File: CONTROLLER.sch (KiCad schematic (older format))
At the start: 25 parts, among them J201 Raspberry_Pi_2_3, Q201 BSS138, Q202 BSS138, U201 MCP23017_SO, U202 MAX11616, U203 MAX3232

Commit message: Review 1
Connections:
- net +5V: now also C202.1; no longer C202.2
- net Earth: now also C202.2; no longer C202.1
- net ILK_CMD renamed ILK_CMD_PI
- net OP renamed OP_CMD_PI
- net RESET_CMD renamed RESET_CMD_PI
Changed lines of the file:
@@
 Sheet 2 4
 Title "RF Amplifier Controller"
-Date "2019-11-23"
+Date "2019-12-01"
 Rev "1"
 Comp "HB9GKW"
@@
 ILK_RF_OL
 Text GLabel 10075 5425 2    50   Output ~ 0
-RESET_CMD
+RESET_CMD_PI
 Text GLabel 3925 7475 0    50   Input ~ 0
 ILK_IDD_OC
@@
 	4925 3675 5050 3675
 Connection ~ 4925 3675
-Wire Wire Line
-	4925 3675 4925 3300
 $Comp
 L power:Earth #PWR?
@@
 	9225 7050 9325 7050
 Text GLabel 10075 5325 2    50   Output ~ 0
-OP
+OP_CMD_PI
 Wire Wire Line
 	10075 5325 9925 5325
 Text GLabel 10075 5525 2    50   Output ~ 0
-ILK_CMD
+ILK_CMD_PI
 Wire Wire Line
 	10075 5525 9925 5525
@@
 AR Path="/5DD09976" Ref="C?"  Part="1"
 AR Path="/5CBD59C6/5DD09976" Ref="C202"  Part="1"
-F 0 "C202" V 4975 3250 50  0000 L CNN
-F 1 "10u" V 5050 3200 50  0000 L CNN
+F 0 "C202" V 5425 3200 50  0000 L CNN
+F 1 "10u" V 5350 3225 50  0000 L CNN
 F 2 "Capacitor_Tantalum_SMD:CP_EIA-6032-28_Kemet-C" H 5238 3150 50  0001 C CNN
 F 3 "~" H 5200 3300 50  0001 C CNN
 	1    5200 3300
-	0    1    1    0
+	0    -1   -1   0
 $EndComp
 $Comp
@@
 	0    -1   -1   0
 $EndComp
-Wire Wire Line
-	5050 3300 4925 3300
-Connection ~ 4925 3300
-Wire Wire Line
-	4925 3300 4925 3175
 Wire Notes Line
 	7925 8050 7925 9825
@@
 	9025 7025 9025 7075
 NoConn ~ 8925 7025
+Wire Wire Line
+	4925 3175 4925 3300
+Wire Wire Line
+	5050 3300 4925 3300
+Connection ~ 4925 3300
+Wire Wire Line
+	4925 3300 4925 3675
 $EndSCHEMATC

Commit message: Review
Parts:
- C202: value 10u -> 47u
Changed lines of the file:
@@
 Sheet 2 4
 Title "RF Amplifier Controller"
-Date "2019-12-01"
+Date "2020-01-19"
 Rev "1"
 Comp "HB9GKW"
@@
 U 1 1 5E639734
 P 5175 5750
-F 0 "C201" V 5400 5650 50  0000 L CNN
-F 1 "100n" V 5325 5650 50  0000 L CNN
+F 0 "C201" V 5375 5650 50  0000 L CNN
+F 1 "100n" V 5300 5650 50  0000 L CNN
 F 2 "Capacitor_SMD:C_0805_2012Metric_Pad1.15x1.40mm_HandSolder" H 5213 5600 50  0001 C CNN
 F 3 "~" H 5175 5750 50  0001 C CNN
@@
 AR Path="/5CBD59C6/5DC48293" Ref="U203"  Part="1"
 AR Path="/5DC48293" Ref="U?"  Part="1"
-F 0 "U203" H 11850 7050 50  0000 C CNN
+F 0 "U203" H 11900 7050 50  0000 C CNN
 F 1 "MAX3232" H 11975 6950 50  0000 C CNN
 F 2 "Package_SO:SOIC-18W_7.5x11.6mm_P1.27mm" H 12450 4850 50  0001 L CNN
@@
 U 1 1 5DC62099
 P 11525 5150
-F 0 "C205" H 11275 5225 50  0000 L CNN
-F 1 "100n" H 11200 5125 50  0000 L CNN
+F 0 "C205" H 11225 5200 50  0000 L CNN
+F 1 "100n" H 11225 5100 50  0000 L CNN
 F 2 "Capacitor_SMD:C_0805_2012Metric_Pad1.15x1.40mm_HandSolder" H 11563 5000 50  0001 C CNN
 F 3 "~" H 11525 5150 50  0001 C CNN
@@
 U 1 1 5DC9523F
 P 13275 5150
-F 0 "C207" H 13025 5225 50  0000 L CNN
-F 1 "100n" H 12950 5125 50  0000 L CNN
+F 0 "C207" H 12975 5200 50  0000 L CNN
+F 1 "100n" H 12975 5100 50  0000 L CNN
 F 2 "Capacitor_SMD:C_0805_2012Metric_Pad1.15x1.40mm_HandSolder" H 13313 5000 50  0001 C CNN
 F 3 "~" H 13275 5150 50  0001 C CNN
@@
 U 1 1 5DE06F4A
 P 13475 5800
-F 0 "C209" V 13600 5975 50  0000 L CNN
+F 0 "C209" V 13600 5875 50  0000 L CNN
 F 1 "100n" V 13525 5875 50  0000 L CNN
 F 2 "Capacitor_SMD:C_0805_2012Metric_Pad1.15x1.40mm_HandSolder" H 13513 5650 50  0001 C CNN
@@
 U 1 1 5DE10581
 P 13475 5500
-F 0 "C208" V 13600 5675 50  0000 L CNN
+F 0 "C208" V 13600 5575 50  0000 L CNN
 F 1 "100n" V 13525 5575 50  0000 L CNN
 F 2 "Capacitor_SMD:C_0805_2012Metric_Pad1.15x1.40mm_HandSolder" H 13513 5350 50  0001 C CNN
@@
 AR Path="/5DE667F3" Ref="R?"  Part="1"
 AR Path="/5CBD59C6/5DE667F3" Ref="R207"  Part="1"
-F 0 "R207" H 9445 8671 50  0000 L CNN
-F 1 "1k8" H 9445 8580 50  0000 L CNN
+F 0 "R207" V 9475 8525 50  0000 L CNN
+F 1 "1k8" V 9550 8550 50  0000 L CNN
 F 2 "Resistor_SMD:R_0805_2012Metric_Pad1.15x1.40mm_HandSolder" V 9305 8625 50  0001 C CNN
 F 3 "~" H 9375 8625 50  0001 C CNN
@@
 AR Path="/5DEA4FD4" Ref="R?"  Part="1"
 AR Path="/5CBD59C6/5DEA4FD4" Ref="R208"  Part="1"
-F 0 "R208" H 9445 9296 50  0000 L CNN
-F 1 "1k8" H 9445 9205 50  0000 L CNN
+F 0 "R208" V 9475 9150 50  0000 L CNN
+F 1 "1k8" V 9550 9175 50  0000 L CNN
 F 2 "Resistor_SMD:R_0805_2012Metric_Pad1.15x1.40mm_HandSolder" V 9305 9250 50  0001 C CNN
 F 3 "~" H 9375 9250 50  0001 C CNN
@@
 AR Path="/5DECE479" Ref="R?"  Part="1"
 AR Path="/5CBD59C6/5DECE479" Ref="R204"  Part="1"
-F 0 "R204" H 8325 8675 50  0000 L CNN
-F 1 "2k7" H 8300 8575 50  0000 L CNN
+F 0 "R204" V 8350 8525 50  0000 L CNN
+F 1 "2k7" V 8425 8550 50  0000 L CNN
 F 2 "Resistor_SMD:R_0805_2012Metric_Pad1.15x1.40mm_HandSolder" V 8430 8625 50  0001 C CNN
 F 3 "~" H 8500 8625 50  0001 C CNN
@@
 AR Path="/5DEE53F9" Ref="R?"  Part="1"
 AR Path="/5CBD59C6/5DEE53F9" Ref="R205"  Part="1"
-F 0 "R205" H 8325 9300 50  0000 L CNN
-F 1 "2k7" H 8300 9200 50  0000 L CNN
+F 0 "R205" V 8350 9150 50  0000 L CNN
+F 1 "2k7" V 8425 9175 50  0000 L CNN
 F 2 "Resistor_SMD:R_0805_2012Metric_Pad1.15x1.40mm_HandSolder" V 8430 9250 50  0001 C CNN
 F 3 "~" H 8500 9250 50  0001 C CNN
@@
 AR Path="/5F47BFDA" Ref="R?"  Part="1"
 AR Path="/5CBD59C6/5F47BFDA" Ref="R202"  Part="1"
-F 0 "R202" H 5900 7500 50  0000 L CNN
-F 1 "2k2" H 5900 7400 50  0000 L CNN
+F 0 "R202" V 5950 7325 50  0000 L CNN
+F 1 "2k2" V 6025 7350 50  0000 L CNN
 F 2 "Resistor_SMD:R_0805_2012Metric_Pad1.15x1.40mm_HandSolder" V 5780 7425 50  0001 C CNN
 F 3 "~" H 5850 7425 50  0001 C CNN
@@
 AR Path="/5F4B73FB" Ref="R?"  Part="1"
 AR Path="/5CBD59C6/5F4B73FB" Ref="R201"  Part="1"
-F 0 "R201" H 5900 7200 50  0000 L CNN
-F 1 "2k2" H 5900 7100 50  0000 L CNN
+F 0 "R201" V 5700 7025 50  0000 L CNN
+F 1 "2k2" V 5775 7050 50  0000 L CNN
 F 2 "Resistor_SMD:R_0805_2012Metric_Pad1.15x1.40mm_HandSolder" V 5780 7125 50  0001 C CNN
 F 3 "~" H 5850 7125 50  0001 C CNN
@@
 U 1 1 5F4E9E98
 P 5900 6675
-F 0 "D201" H 6050 6425 50  0000 C CNN
-F 1 "BAT54AW" H 6100 6500 50  0000 C CNN
+F 0 "D201" H 5475 6650 50  0000 C CNN
+F 1 "BAT54AW" H 5400 6750 50  0000 C CNN
 F 2 "Package_TO_SOT_SMD:SOT-323_SC-70" H 5975 6800 50  0001 L CNN
 F 3 "https://assets.nexperia.com/documents/data-sheet/BAT54W_SER.pdf" H 5780 6675 50  0001 C CNN
@@
 AR Path="/5F5070BD" Ref="R?"  Part="1"
 AR Path="/5CBD59C6/5F5070BD" Ref="R203"  Part="1"
-F 0 "R203" H 6245 6296 50  0000 L CNN
-F 1 "1k5" H 6245 6205 50  0000 L CNN
+F 0 "R203" V 6275 6150 50  0000 L CNN
+F 1 "1k5" V 6350 6175 50  0000 L CNN
 F 2 "Resistor_SMD:R_0805_2012Metric_Pad1.15x1.40mm_HandSolder" V 6105 6250 50  0001 C CNN
 F 3 "~" H 6175 6250 50  0001 C CNN
@@
 AR Path="/5CBD59C6/5DD09976" Ref="C202"  Part="1"
 F 0 "C202" V 5425 3200 50  0000 L CNN
-F 1 "10u" V 5350 3225 50  0000 L CNN
+F 1 "47u" V 5350 3225 50  0000 L CNN
 F 2 "Capacitor_Tantalum_SMD:CP_EIA-6032-28_Kemet-C" H 5238 3150 50  0001 C CNN
 F 3 "~" H 5200 3300 50  0001 C CNN

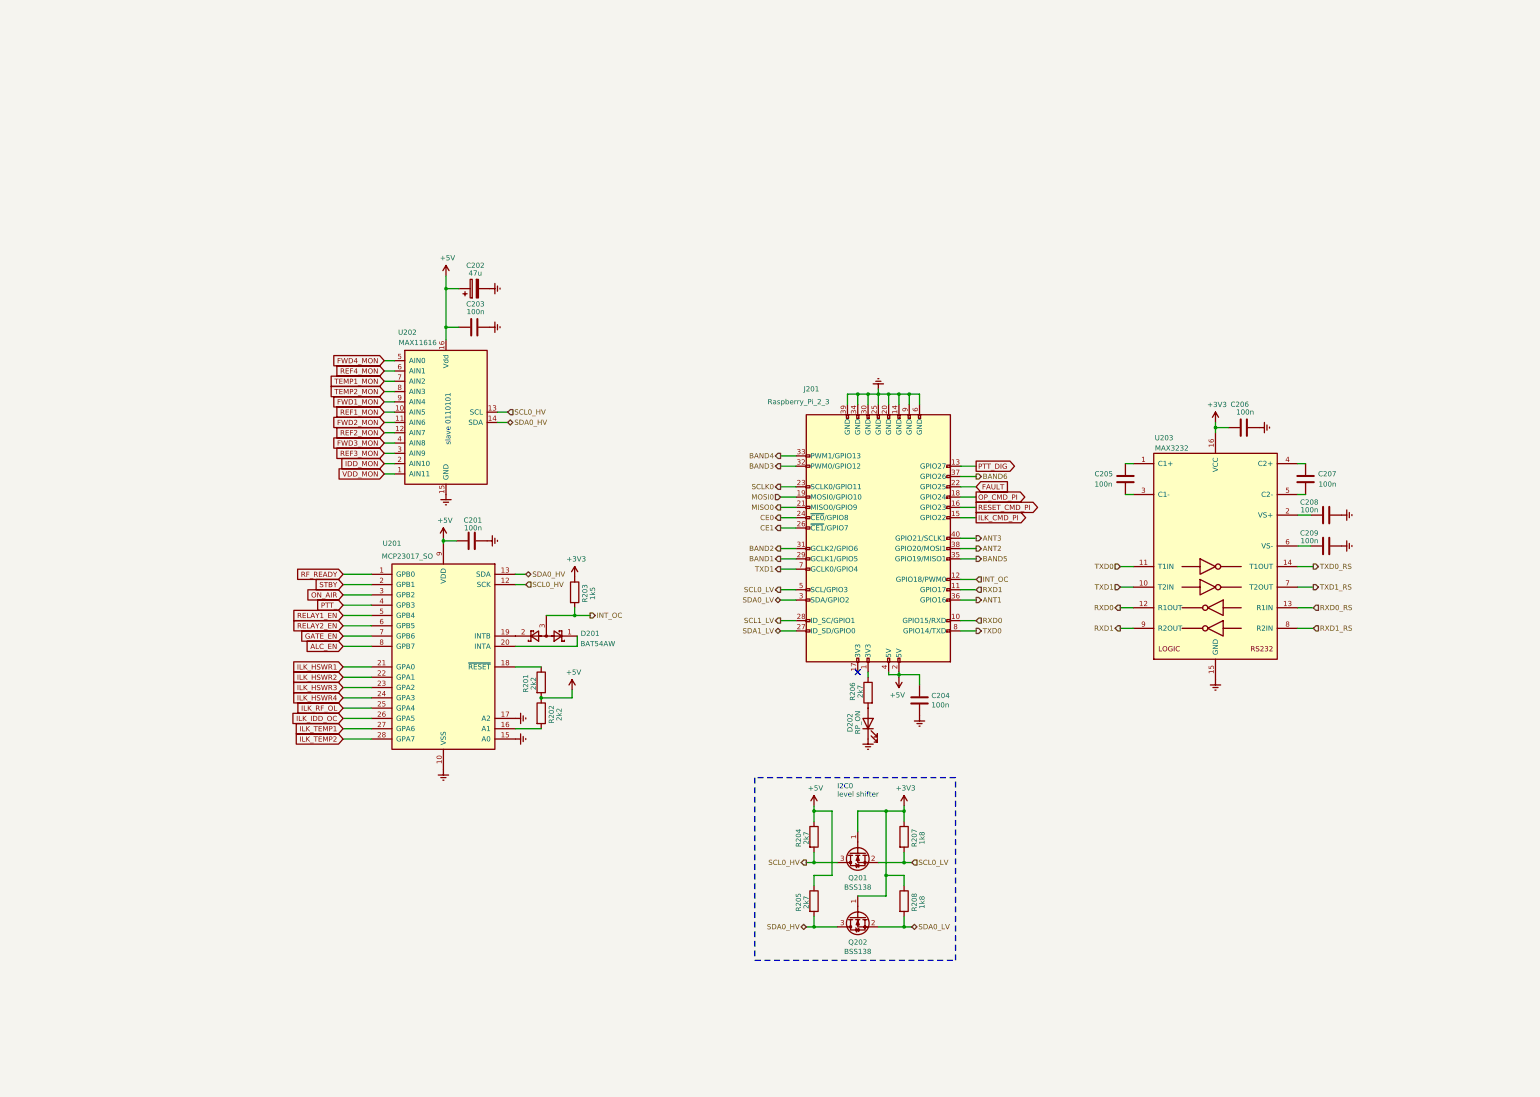
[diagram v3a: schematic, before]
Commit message: new Version with AVR Controller
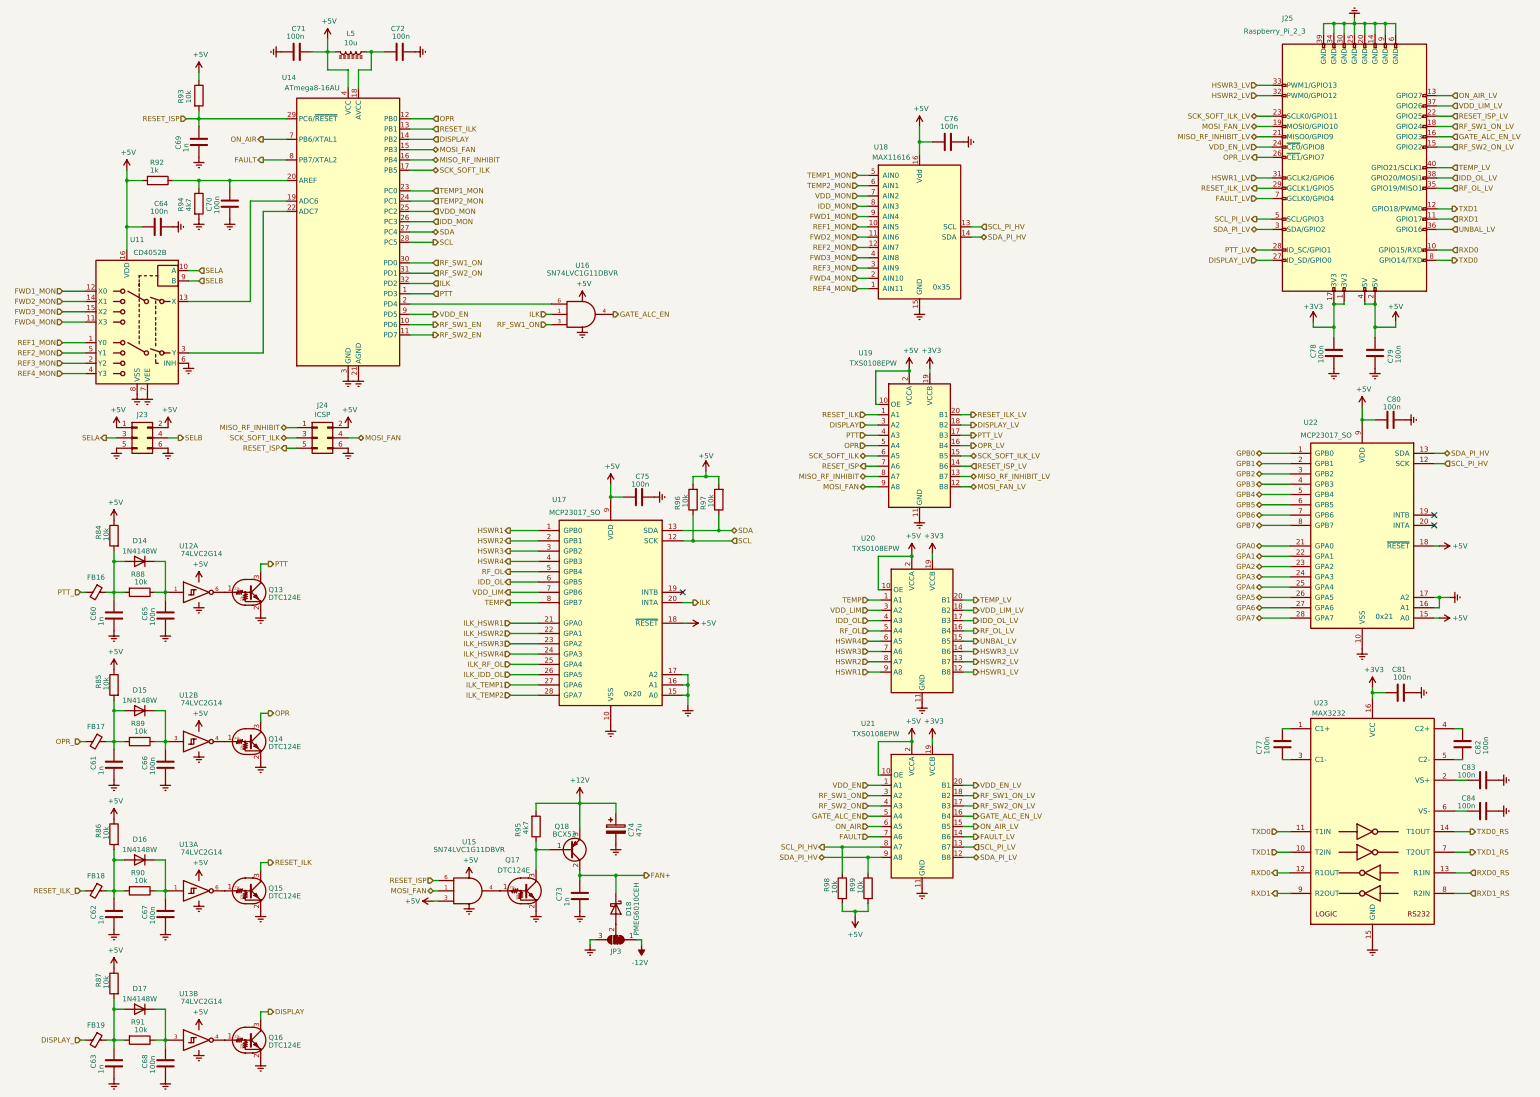
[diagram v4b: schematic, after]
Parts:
- removed C202: 47u, Capacitor_Tantalum_SMD:CP_EIA-6032-28_Kemet-C, symbol Device:CP
- removed D201: BAT54AW, Package_TO_SOT_SMD:SOT-323_SC-70, symbol Diode:BAT54AW
- removed D202: RP_ON, LED_THT:LED_D3.0mm, symbol Device:LED
- removed Q201, Q202: BSS138, Package_TO_SOT_SMD:SOT-23, symbol Transistor_FET:BSS138
- removed R201, R202: 2k2, Resistor_SMD:R_0805_2012Metric_Pad1.15x1.40mm_HandSolder, symbol Device:R
- removed R203: 1k5, Resistor_SMD:R_0805_2012Metric_Pad1.15x1.40mm_HandSolder, symbol Device:R
- removed R204, R205, R206: 2k7, Resistor_SMD:R_0805_2012Metric_Pad1.15x1.40mm_HandSolder, symbol Device:R
- removed R207, R208: 1k8, Resistor_SMD:R_0805_2012Metric_Pad1.15x1.40mm_HandSolder, symbol Device:R
- added C60, C61, C62, C63, C69, C73: 1n, Capacitor_SMD:C_0805_2012Metric_Pad1.15x1.40mm_HandSolder, symbol Device:C
- added C64, C65, C66, C67, C68, C70, C71, C72, C78, C80: 100n, Capacitor_SMD:C_0805_2012Metric_Pad1.15x1.40mm_HandSolder, symbol Device:C
- added C74: 47u, Capacitor_Tantalum_SMD:CP_EIA-6032-28_Kemet-C, symbol Device:CP
- added D14, D15, D16, D17: 1N4148W, Diode_SMD:D_SOD-123, symbol Diode:1N4148W
- added D18: PMEG6010CEH, Diode_SMD:D_SOD-123, symbol Diode:PMEG6010CEH
- added FB16, FB17, FB18, FB19: Ferrite_Bead_Small, Resistor_SMD:R_0805_2012Metric_Pad1.15x1.40mm_HandSolder, symbol Device:Ferrite_Bead_Small
- added J23: Conn_02x03_Odd_Even, Connector_PinHeader_2.54mm:PinHeader_2x03_P2.54mm_Vertical, symbol Connector_Generic:Conn_02x03_Odd_Even
- added J24: ICSP, Connector_PinHeader_2.54mm:PinHeader_2x03_P2.54mm_Vertical, symbol Connector_Generic:Conn_02x03_Odd_Even
- added JP3: SolderJumper_3_Bridged12, Jumper:SolderJumper-3_P1.3mm_Open_RoundedPad1.0x1.5mm, symbol Jumper:SolderJumper_3_Bridged12
- added L5: 10u, Inductor_SMD:L_0805_2012Metric, symbol Device:L_Core_Ferrite
- added Q13, Q14, Q15, Q16, Q17: DTC124E, Package_TO_SOT_SMD:SOT-23, symbol Transistor_BJT:DTC124E
- added Q18: BCX53, Package_TO_SOT_SMD:SOT-89-3, symbol Transistor_BJT:BCX53
- added R84, R85, R86, R87, R88, R89, R90, R91, R93, R96, R97, R98, R99: 10k, Resistor_SMD:R_0805_2012Metric_Pad1.15x1.40mm_HandSolder, symbol Device:R
- added R92: 1k, Resistor_SMD:R_0805_2012Metric_Pad1.15x1.40mm_HandSolder, symbol Device:R
- added R94, R95: 4k7, Resistor_SMD:R_0805_2012Metric_Pad1.15x1.40mm_HandSolder, symbol Device:R
- added U11: CD4052B, Package_SO:SOIC-16_3.9x9.9mm_P1.27mm, symbol Analog_Switch:CD4052B
- added U12, U13: 74LVC2G14, Package_TO_SOT_SMD:SOT-23-6, symbol 74xGxx:74LVC2G14
- added U14: ATmega8-16AU, Package_QFP:TQFP-32_7x7mm_P0.8mm, symbol MCU_Microchip_ATmega:ATmega8-16AU
- added U15, U16: SN74LVC1G11DBVR, Package_TO_SOT_SMD:SOT-23-6, symbol 74xGxx:74LVC1G11
- added U19, U20, U21: TXS0108EPW, Package_SO:TSSOP-20_4.4x6.5mm_P0.65mm, symbol Logic_LevelTranslator:TXS0108EPW
- added U22: MCP23017_SO, Package_SO:SOIC-28W_7.5x17.9mm_P1.27mm, symbol Interface_Expansion:MCP23017_SO
- renumbered C201 to C75, C203 to C76, C205 to C77, C204 to C79, C206 to C81, C207 to C82, C208 to C83, C209 to C84, J201 to J25, U201 to U17, U202 to U18, U203 to U23
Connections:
- net INT_OC is gone; now on net TXD1: J25.12 (GPIO18/PWM0)
- net +3V3: now also J25.1 (3V3), J25.17 (3V3), C78.1, U19.19 (VCCB), U20.19 (VCCB), U21.19 (VCCB)
- net +5V: now also U17.18 (~RESET~), C64.1, C71.1, C80.1, J23.1 (Pin_1), J23.2 (Pin_2), J24.2 (Pin_2), L5.2, R84.1, R85.1, R86.1, R87.1, R92.2, R93.1, R96.2, R97.2, R98.2, R99.2, U11.16 (VDD), U12.5 (VCC), U12.5 (VCC), U13.5 (VCC), U13.5 (VCC), U14.4 (VCC), U14.6 (VCC), U15.3, U15.5 (VCC), U16.5 (VCC), U19.10 (OE), U19.2 (VCCA), U20.10 (OE), U20.2 (VCCA), U21.10 (OE), U21.2 (VCCA), U22.15 (A0), U22.18 (~RESET~), U22.9 (VDD)
- net Earth: now also U17.16 (A1), C60.2, C61.2, C62.2, C63.2, C64.2, C65.2, C66.2, C67.2, C68.2, C69.2, C70.2, C71.2, C72.2, C73.2, C74.2, C78.2, C80.2, J23.5 (Pin_5), J23.6 (Pin_6), J24.6 (Pin_6), JP3.3 (B), Q13.2 (E), Q14.2 (E), Q15.2 (E), Q16.2 (E), Q17.2 (E), R94.2, U11.6 (INH), U11.7 (VEE), U11.8 (VSS), U12.2 (GND), U12.2 (GND), U13.2 (GND), U13.2 (GND), U14.21 (AGND), U14.3 (GND), U14.5 (GND), U15.2 (GND), U16.2 (GND), U19.11 (GND), U20.11 (GND), U21.11 (GND), U22.10 (VSS), U22.16 (A1), U22.17 (A2)
- net FAULT: now also U14.8 (PB7/XTAL2), U21.7 (A6); no longer J25.22 (GPIO25)
- net FWD1_MON: now also U11.12 (X0)
- net FWD2_MON: now also U11.14 (X1)
- net FWD3_MON: now also U11.15 (X2)
- net FWD4_MON: now also U18.2 (AIN10), U11.11 (X3); no longer U18.5 (AIN0)
- net IDD_MON: now also U18.8 (AIN3), U14.26 (PC3); no longer U18.2 (AIN10)
- net ON_AIR: now also U14.7 (PB6/XTAL1), U21.6 (A5); no longer U17.3 (GPB2)
- net PTT_: now also FB16.2; no longer U17.4 (GPB3)
- net REF1_MON: now also U11.1 (Y0)
- net REF2_MON: now also U11.5 (Y1)
- net REF3_MON: now also U11.2 (Y2)
- net REF4_MON: now also U18.1 (AIN11), U11.4 (Y3); no longer U18.6 (AIN1)
- net TEMP1_MON: now also U18.5 (AIN0), U14.23 (PC0); no longer U18.7 (AIN2)
- net TEMP2_MON: now also U18.6 (AIN1), U14.24 (PC1); no longer U18.8 (AIN3)
- net TXD1: no longer J25.7 (GCLK0/GPIO4)
- net VDD_MON: now also U18.7 (AIN2), U14.25 (PC2); no longer U18.1 (AIN11)
- net ILK: now reaches U17.20 (INTA)
- net ILK: now also U14.32 (PD2), U16.1
- net ALC_EN renamed TEMP
- net TEMP: now also U20.1 (A1)
- net ANT1 renamed UNBAL_LV
- net UNBAL_LV: now also U20.15 (B5)
- net ANT2 renamed IDD_OL_LV
- net IDD_OL_LV: now also U20.17 (B3)
- net ANT3 renamed TEMP_LV
- net TEMP_LV: now also U20.20 (B1)
- net BAND1 renamed RESET_ILK_LV
- net RESET_ILK_LV: now also U19.20 (B1)
- net BAND2 renamed HSWR1_LV
- net HSWR1_LV: now also U20.12 (B8)
- net BAND3 renamed HSWR2_LV
- net HSWR2_LV: now also U20.13 (B7)
- net BAND4 renamed HSWR3_LV
- net HSWR3_LV: now also U20.14 (B6)
- net BAND5 renamed RF_OL_LV
- net RF_OL_LV: now also U20.16 (B4)
- net BAND6 renamed VDD_LIM_LV
- net VDD_LIM_LV: now also U20.18 (B2)
- net CE0 renamed VDD_EN_LV
- net VDD_EN_LV: now also U21.20 (B1)
- net CE1 renamed OPR_LV
- net OPR_LV: now also U19.16 (B4)
- net GATE_EN renamed VDD_LIM
- net VDD_LIM: now also U20.3 (A2)
- net ILK_CMD_PI renamed RF_SW2_ON_LV
- net RF_SW2_ON_LV: now also U21.17 (B3)
- net ILK_IDD_OC renamed ILK_IDD_OL
- net MISO0 renamed MISO_RF_INHIBIT_LV
- net MISO_RF_INHIBIT_LV: now also U19.13 (B7)
- net MOSI0 renamed MOSI_FAN_LV
- net MOSI_FAN_LV: now also U19.12 (B8)
- net OP_CMD_PI renamed RF_SW1_ON_LV
- net RF_SW1_ON_LV: now also U21.18 (B2)
- net PTT_DIG renamed ON_AIR_LV
- net ON_AIR_LV: now also U21.15 (B5)
- net RELAY1_EN renamed RF_OL
- net RF_OL: now also U20.5 (A4)
- net RELAY2_EN renamed IDD_OL
- net IDD_OL: now also U20.4 (A3)
- net RESET_CMD_PI renamed GATE_ALC_EN_LV
- net GATE_ALC_EN_LV: now also U21.16 (B4)
- net RF_READY renamed HSWR1
- net HSWR1: now also U20.9 (A8)
- net SCL0_HV renamed SCL
- net SCL: now also R96.1, U14.28 (PC5); no longer U18.13 (SCL)
- net SCL0_LV renamed SCL_PI_LV
- net SCL_PI_LV: now also U21.13 (B7)
- net SCL1_LV renamed PTT_LV
- net PTT_LV: now also U19.17 (B3)
- net SCLK0 renamed SCK_SOFT_ILK_LV
- net SCK_SOFT_ILK_LV: now also U19.15 (B5)
- net SDA0_HV renamed SDA
- net SDA: now also R97.1, U14.27 (PC4); no longer U18.14 (SDA)
- net SDA0_LV renamed SDA_PI_LV
- net SDA_PI_LV: now also U21.12 (B8)
- net SDA1_LV renamed DISPLAY_LV
- net DISPLAY_LV: now also U19.18 (B2)
- net STBY renamed HSWR2
- net HSWR2: now also U20.8 (A7)
- new net: C72.1, L5.1, U14.18 (AVCC)
- new net: U11.13 (X), U14.19 (ADC6)
- new net: U14.2 (PD4), U16.6
- new net: C70.1, R92.1, R94.1, U14.20 (AREF)
- new net: U11.3 (Y), U14.22 (ADC7)
- new net: Q17.1 (B), U15.4
- new net: Q17.3 (C), Q18.1 (B), R95.1
- new net: D18.2 (A), JP3.2 (C)
- new net: C60.1, D14.2 (A), FB16.1, R84.2, R88.2
- new net: C65.1, D14.1 (K), R88.1, U12.1
- new net: C61.1, D15.2 (A), FB17.1, R85.2, R89.2
- new net: C66.1, D15.1 (K), R89.1, U12.3
- new net: C62.1, D16.2 (A), FB18.1, R86.2, R90.2
- new net: C67.1, D16.1 (K), R90.1, U13.1
- new net: C63.1, D17.2 (A), FB19.1, R87.2, R91.2
- new net: C68.1, D17.1 (K), R91.1, U13.3
- new net: Q13.1 (B), U12.6
- new net: Q14.1 (B), U12.4
- new net: Q15.1 (B), U13.6
- new net: Q16.1 (B), U13.4
- new net +12V: C74.1, Q18.3 (E), R95.2
- new net -12V: JP3.1 (A)
- new net DISPLAY: Q16.3 (C), U14.14 (PB2), U19.3 (A2)
- new net DISPLAY_: FB19.2
- new net FAN+: C73.1, D18.1 (K), Q18.2 (C)
- new net FAULT_LV: J25.7 (GCLK0/GPIO4), U21.14 (B6)
- new net GATE_ALC_EN: U16.4, U21.5 (A4)
- new net GPA0: U22.21 (GPA0)
- new net GPA1: U22.22 (GPA1)
- new net GPA2: U22.23 (GPA2)
- new net GPA3: U22.24 (GPA3)
- new net GPA4: U22.25 (GPA4)
- new net GPA5: U22.26 (GPA5)
- new net GPA6: U22.27 (GPA6)
- new net GPA7: U22.28 (GPA7)
- new net GPB0: U22.1 (GPB0)
- new net GPB1: U22.2 (GPB1)
- new net GPB2: U22.3 (GPB2)
- new net GPB3: U22.4 (GPB3)
- new net GPB4: U22.5 (GPB4)
- new net GPB5: U22.6 (GPB5)
- new net GPB6: U22.7 (GPB6)
- new net GPB7: U22.8 (GPB7)
- new net HSWR3: U17.3 (GPB2), U20.7 (A6)
- new net HSWR4: U17.4 (GPB3), U20.6 (A5)
- new net MISO_RF_INHIBIT: J24.1 (Pin_1), U14.16 (PB4), U19.8 (A7)
- new net MOSI_FAN: J24.4 (Pin_4), U14.15 (PB3), U15.1, U19.9 (A8)
- new net OPR: Q14.3 (C), U14.12 (PB0), U19.5 (A4)
- new net OPR_: FB17.2
- new net PTT: Q13.3 (C), U14.1 (PD3), U19.4 (A3)
- new net RESET_ILK: Q15.3 (C), U14.13 (PB1), U19.1 (A1)
- new net RESET_ILK_: FB18.2
- new net RESET_ISP: C69.1, J24.5 (Pin_5), R93.2, U14.29 (PC6/~RESET), U15.6, U19.7 (A6)
- new net RESET_ISP_LV: J25.22 (GPIO25), U19.14 (B6)
- new net RF_SW1_EN: U14.10 (PD6)
- new net RF_SW1_ON: U14.30 (PD0), U16.3, U21.3 (A2)
- new net RF_SW2_EN: U14.11 (PD7)
- new net RF_SW2_ON: U14.31 (PD1), U21.4 (A3)
- new net SCK_SOFT_ILK: J24.3 (Pin_3), U14.17 (PB5), U19.6 (A5)
- new net SCL_PI_HV: R98.1, U18.13 (SCL), U21.8 (A7), U22.12 (SCK)
- new net SDA_PI_HV: R99.1, U18.14 (SDA), U21.9 (A8), U22.13 (SDA)
- new net SELA: J23.3 (Pin_3), U11.10 (A)
- new net SELB: J23.4 (Pin_4), U11.9 (B)
- new net VDD_EN: U14.9 (PD5), U21.1 (A1)
- no-connect marks 1 -> 3
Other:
- note added: "0x20"
- note added: "0x21"
- note added: "0x35"
- note removed: "I2C0\nlevel shifter"
- note removed: "slave 0110101"
- moved on the sheet: C75, C76, C77, C79, C81, C82, C83, C84, J25, U17, U18, U23

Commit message: RC1
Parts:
- C65: value 100n -> 10n
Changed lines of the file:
@@
 AR Path="/5CBD59C6/5FB02049" Ref="C65"  Part="1"
 F 0 "C65" V 2400 6425 50  0000 L CNN
-F 1 "100n" V 2325 6375 50  0000 L CNN
+F 1 "10n" V 2325 6375 50  0000 L CNN
 F 2 "Capacitor_SMD:C_0805_2012Metric_Pad1.15x1.40mm_HandSolder" H 2238 6325 50  0001 C CNN
 F 3 "~" H 2200 6475 50  0001 C CNN

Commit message: RC2
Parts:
- added R102: 110, Resistor_SMD:R_0805_2012Metric_Pad1.15x1.40mm_HandSolder, symbol Device:R
- renumbered R98 to R100, R99 to R101, R84 to R86, R85 to R87, R86 to R88, R87 to R89, R88 to R90, R89 to R91, R90 to R92, R91 to R93, R92 to R94, R93 to R95, R94 to R96, R95 to R97, R96 to R98, R97 to R99
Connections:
- net at Q18.1 (B), R97.1: now also R102.2; no longer Q17.3 (C)
- new net: Q17.3 (C), R102.1
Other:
- moved on the sheet: Q17, U15
